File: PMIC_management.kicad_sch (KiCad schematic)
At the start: 25 parts, among them SW1 SKSGPAE010, SW2 SKSGPAE010, U3 RK809-2, Y2 32.768kHz ±20ppm 12.5pF

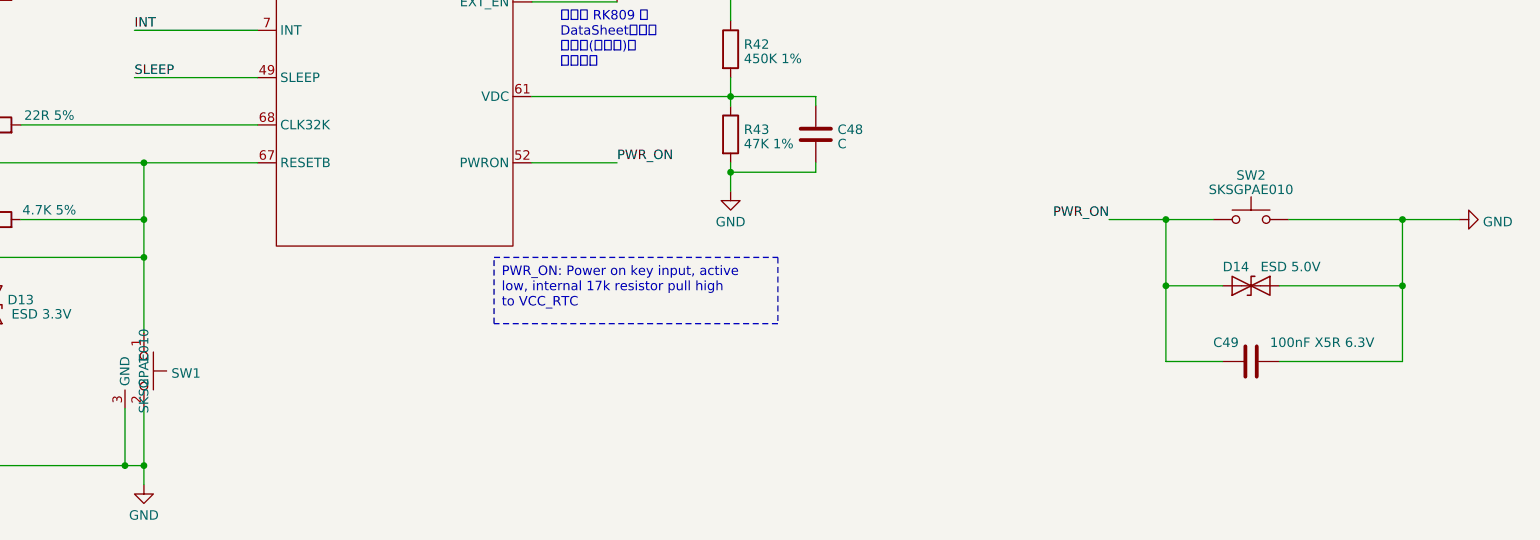
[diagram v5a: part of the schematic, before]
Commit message: updated PMIC
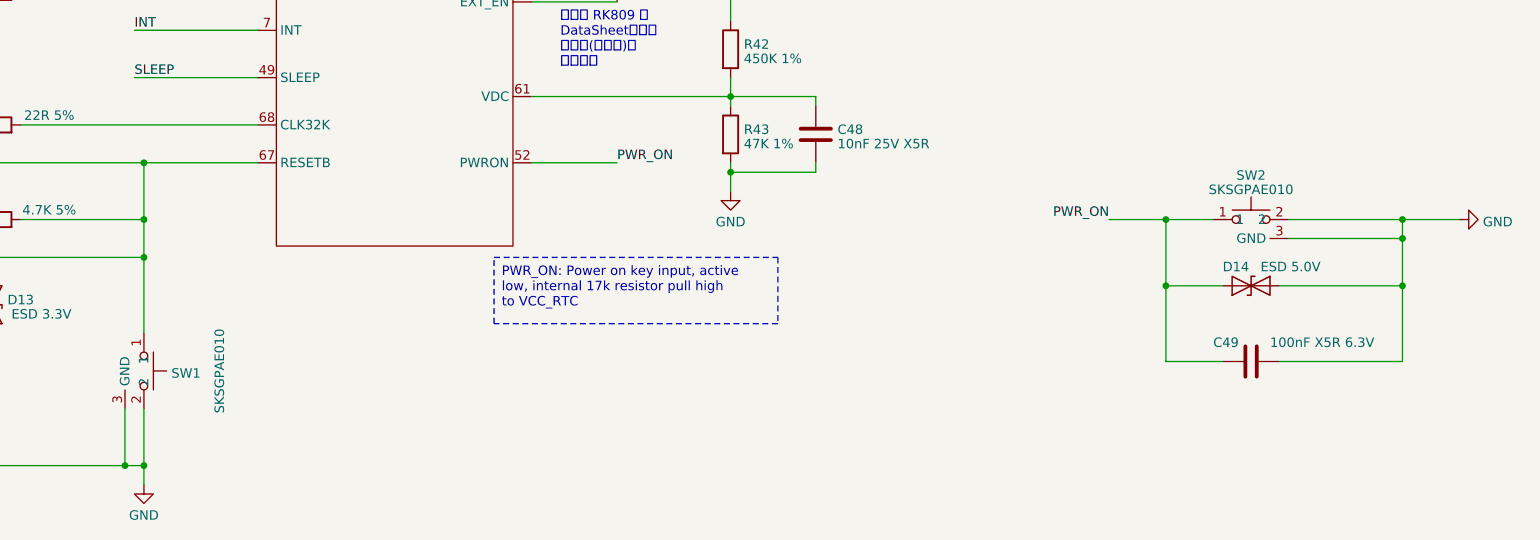
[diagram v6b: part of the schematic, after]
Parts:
- C48: value C -> 10nF 25V X5R; footprint Capacitor_SMD:C_0603_1608Metric -> Capacitor_SMD:C_0402_1005Metric; LCSC (none) -> C327025; Model (none) -> CC0402KRX7R8BB103; Vendor (none) -> YAGEO(国巨)
- SW2: symbol Switch:SW_Push -> Leaf_Switch:SW_Push_SPST
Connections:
- net GND: now also SW2.3 (GND)
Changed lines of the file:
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@@
   (junction (at 166.37 109.22) (diameter 0) (color 0 0 0 0)
   )
+  (junction (at 256.54 118.11) (diameter 0) (color 0 0 0 0)
+  )
   (junction (at 224.79 58.42) (diameter 0) (color 0 0 0 0)
   )
@@
     (stroke (width 0) (type default))
   )
-  (wire (pts (xy 256.54 124.46) (xy 256.54 115.57))
+  (wire (pts (xy 256.54 124.46) (xy 256.54 118.11))
+    (stroke (width 0) (type default))
+  )
+  (wire (pts (xy 241.3 118.11) (xy 256.54 118.11))
     (stroke (width 0) (type default))
   )
@@
   )
   (wire (pts (xy 177.8 99.06) (xy 166.37 99.06))
+    (stroke (width 0) (type default))
+  )
+  (wire (pts (xy 256.54 118.11) (xy 256.54 115.57))
     (stroke (width 0) (type default))
   )
@@
     )
   )
-  (symbol (lib_id "Switch:SW_Push") (at 236.22 115.57 0) (unit 1)
+  (symbol (lib_id "Leaf_Switch:SW_Push_SPST") (at 236.22 115.57 0) (unit 1)
     (in_bom yes) (on_board yes) (dnp no) (fields_autoplaced)
     (property "Reference" "SW2" (at 236.22 109.6391 0)
@@
       (effects (font (size 1.27 1.27)))
     )
-    (property "Footprint" "Leaf_Button_Switch_SMD:SW_SPST_ALPS_SKSG_3.9x2.7mm" (at 236.22 110.49 0)
-      (effects (font (size 1.27 1.27)) hide)
-    )
-    (property "Datasheet" "~" (at 236.22 110.49 0)
+    (property "Footprint" "Leaf_Button_Switch_SMD:SW_SPST_ALPS_SKSG_3.9x2.7mm" (at 236.22 115.57 0)
+      (effects (font (size 1.27 1.27)) hide)
+    )
+    (property "Datasheet" "~" (at 236.22 115.57 0)
       (effects (font (size 1.27 1.27)) hide)
     )
@@
     (pin "1")
     (pin "2")
+    (pin "3")
     (instances
       (project "leaf"
@@
   )
   (symbol (lib_id "Leaf_Switch:SW_Push_SPST") (at 87.63 135.89 270) (unit 1)
-    (in_bom yes) (on_board yes) (dnp no) (fields_autoplaced)
+    (in_bom yes) (on_board yes) (dnp no)
     (property "Reference" "SW1" (at 91.313 136.2068 90)
       (effects (font (size 1.27 1.27)) (justify left))
     )
-    (property "Value" "SKSGPAE010" (at 87.63 135.89 0)
+    (property "Value" "SKSGPAE010" (at 97.79 135.89 0)
       (effects (font (size 1.27 1.27)))
     )
@@
       (effects (font (size 1.27 1.27)) (justify left))
     )
-    (property "Value" "C" (at 180.721 105.4173 0)
-      (effects (font (size 1.27 1.27)) (justify left))
-    )
-    (property "Footprint" "Capacitor_SMD:C_0603_1608Metric" (at 178.7652 107.95 0)
+    (property "Value" "10nF 25V X5R" (at 180.721 105.4173 0)
+      (effects (font (size 1.27 1.27)) (justify left))
+    )
+    (property "Footprint" "Capacitor_SMD:C_0402_1005Metric" (at 178.7652 107.95 0)
       (effects (font (size 1.27 1.27)) hide)
     )
@@
       (effects (font (size 1.27 1.27)) hide)
     )
+    (property "Description" "容值: 10nF 精度: ±10% 额定电压: 25V 材质(温度系数): X7R 材质:X7R" (at 177.8 104.14 0)
+      (effects (font (size 1.27 1.27)) hide)
+    )
+    (property "LCSC" "C327025" (at 177.8 104.14 0)
+      (effects (font (size 1.27 1.27)) hide)
+    )
+    (property "Model" "CC0402KRX7R8BB103" (at 177.8 104.14 0)
+      (effects (font (size 1.27 1.27)) hide)
+    )
+    (property "Vendor" "YAGEO(国巨)" (at 177.8 104.14 0)
+      (effects (font (size 1.27 1.27)) hide)
+    )

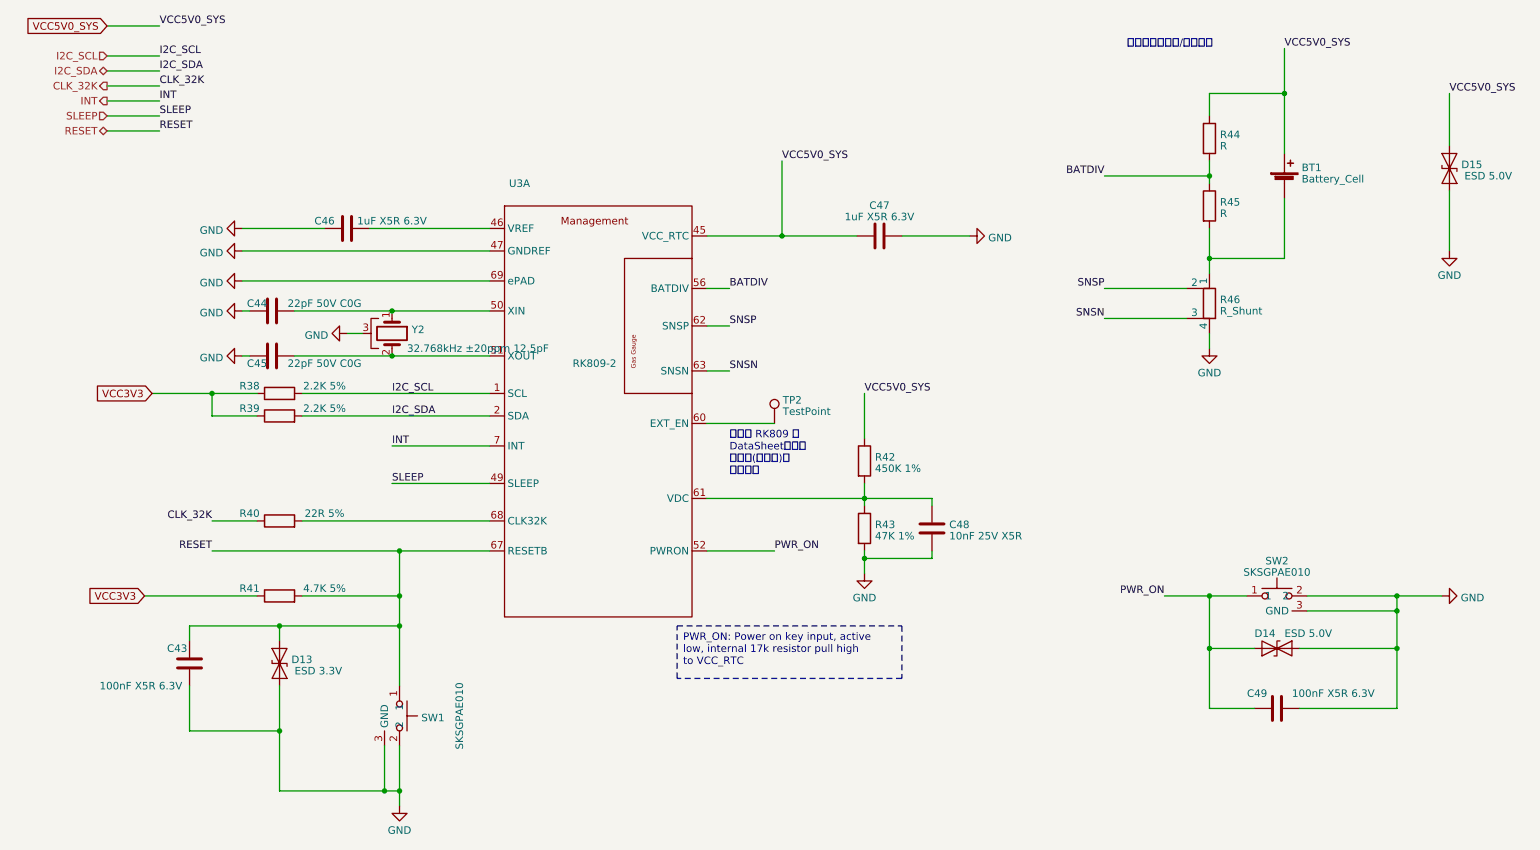
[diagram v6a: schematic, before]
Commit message: fix some ERCs
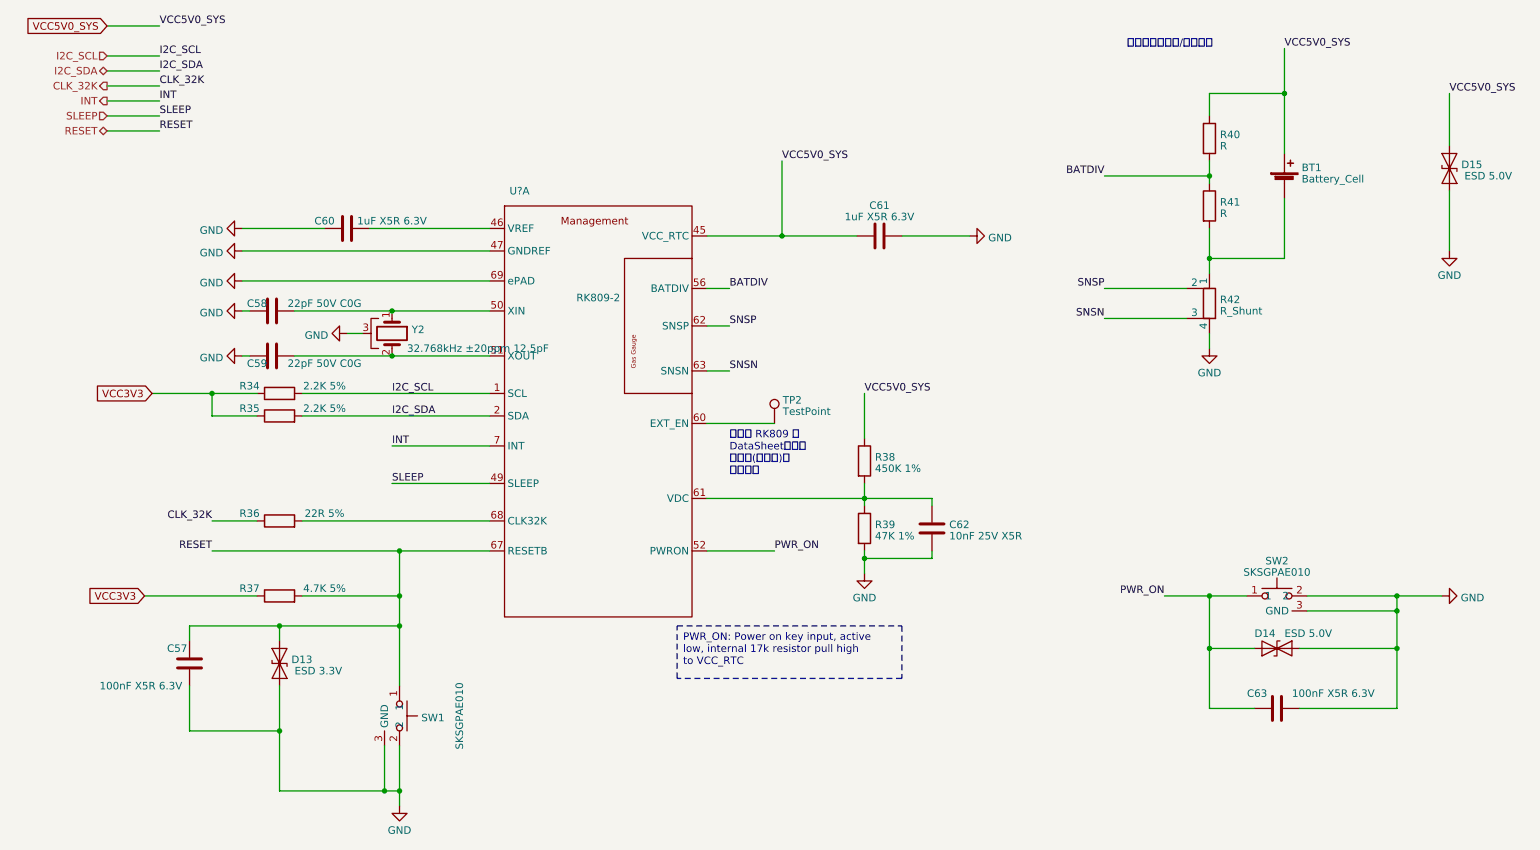
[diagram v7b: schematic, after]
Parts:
- renumbered C43 to C57, C44 to C58, C45 to C59, C46 to C60, C47 to C61, C48 to C62, C49 to C63, R38 to R34, R39 to R35, R40 to R36, R41 to R37, R42 to R38, R43 to R39, R44 to R40, R45 to R41, R46 to R42, U3 to U?
